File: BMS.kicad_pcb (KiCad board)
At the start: 2 copper layers, 129 parts, among them IC1 AOZ2261NQI-11, IC2 AOZ2261NQI-11, IC2 LM2596DSADJG, IC3 AOZ2261NQI-11, IC4 AOZ2261NQI-11, IC5 AOZ2261NQI-11, IC6 AOZ2261NQI-11, IC7 AOZ2261NQI-11, J1 Conn_01x05_Pin, J10 XT90PB-F, J11 XT90PB-F, J12 XT90PB-F, J2 XT90PB-F, J3 Conn_01x02_Pin, J4 Conn_01x03_Pin, J5 XT90PB-F, J6 XT90PB-F, J7 XT90PB-F, J8 XT90PB-F, J9 XT90PB-F, Q1 BSC028N06LS3, Q2 IRLB3813PBF, U1 BQ76920PW, U2 453-00001R

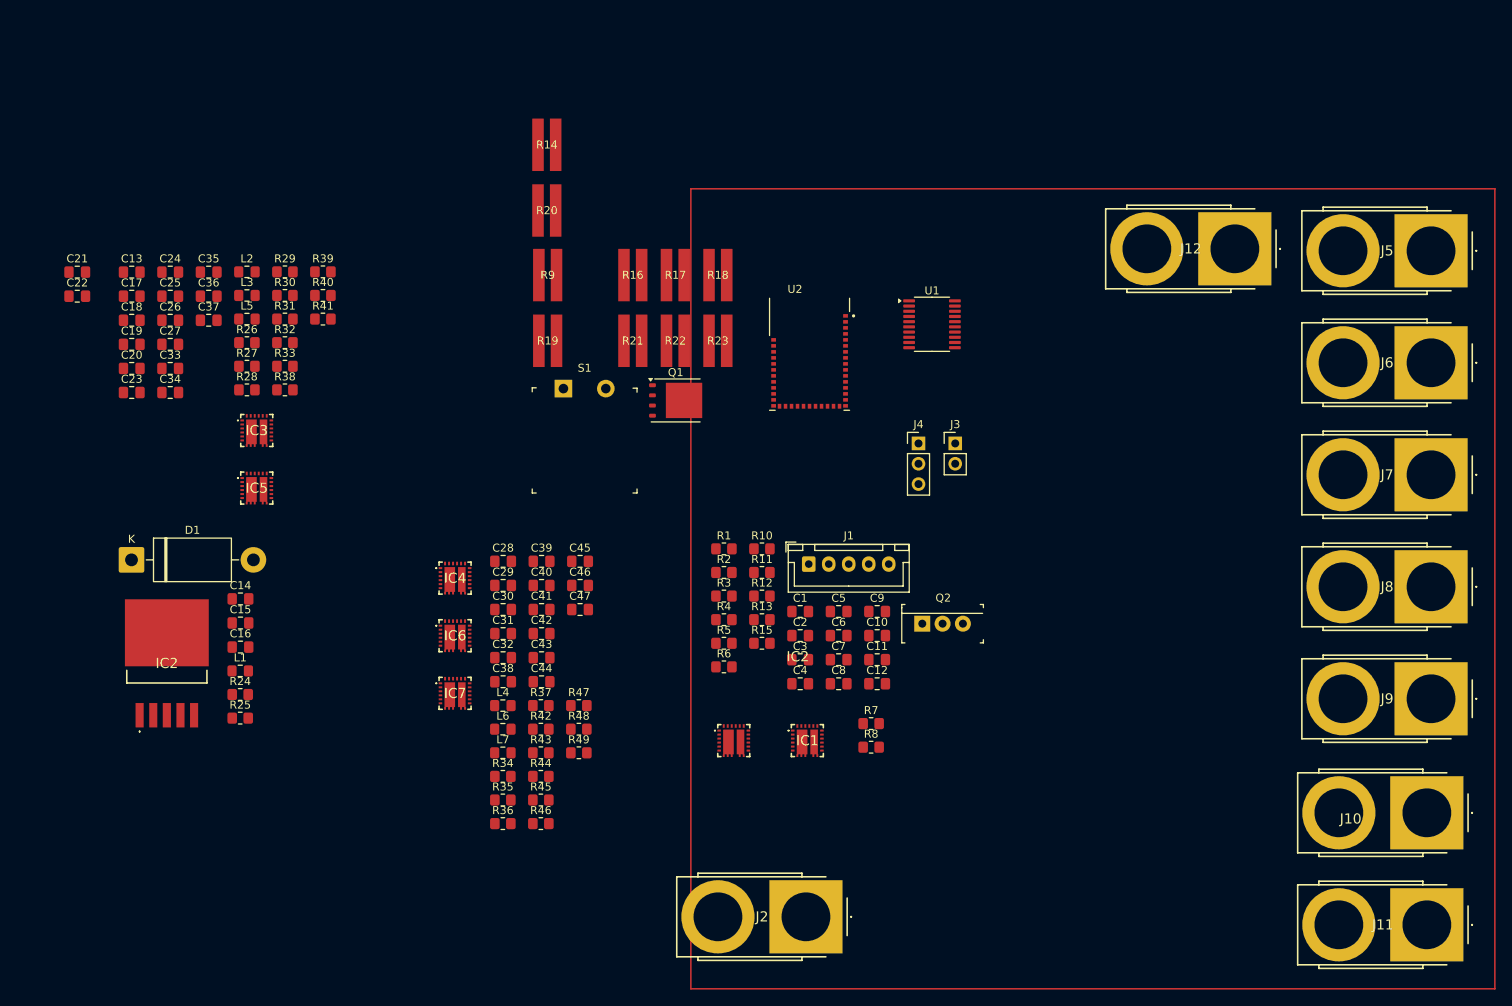
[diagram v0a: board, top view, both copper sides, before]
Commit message: Added output and input caps for buck converters into the schematic. Added components into the project specific library.
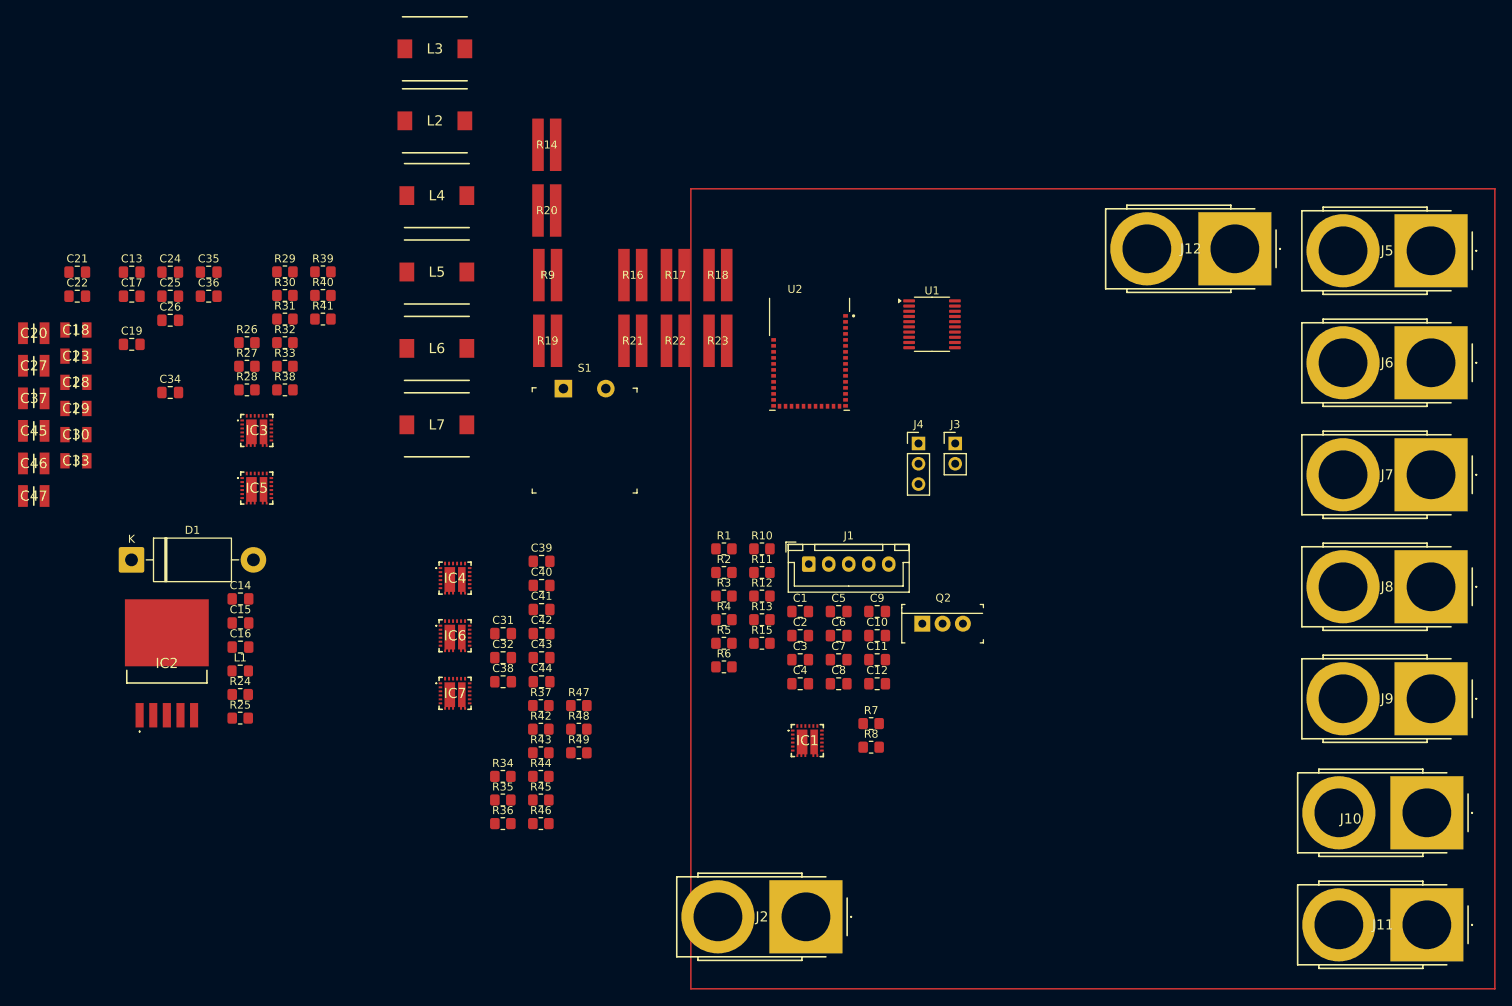
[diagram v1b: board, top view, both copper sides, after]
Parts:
- removed the IC2 at (108.4, 100.5)
- removed Q1: BSC028N06LS3, Package_TO_SOT_SMD:TDSON-8-1
- C18, C23, C28, C29, C30, C33: value 22u -> TMK316BBJ226ML-T; footprint Capacitor_SMD:C_0805_2012Metric_Pad1.18x1.45mm_HandSolder -> TMK316BBJ226ML-T:CAPC3216X190N
- C20, C27, C37, C45, C46, C47: value 22u -> EMK325ABJ107MM-P; footprint Capacitor_SMD:C_0805_2012Metric_Pad1.18x1.45mm_HandSolder -> EMK325ABJ107MM-P:CAPC3225X270N
- L2, L3, L4, L5, L6, L7: value 1u -> HCM1A0805-3R3-R; footprint Inductor_SMD:L_0805_2012Metric_Pad1.15x1.40mm_HandSolder -> HCM1A0805-3R3-R:INDPM8180X540N
- moved C45 70.2 mm to (20.9, 61.8)
- moved C46 70.0 mm to (20.9, 65.8)
- moved C47 69.7 mm to (20.9, 69.9)
- moved L4 64.3 mm to (71.2, 32.4)
- moved C28 57.9 mm to (26.1, 55.7)
- moved C29 57.8 mm to (26.1, 59.0)
- moved C30 57.7 mm to (26.1, 62.2)
- moved L6 48.3 mm to (71.2, 51.5)
- moved L7 41.8 mm to (71.2, 61.0)
- moved L3 38.8 mm to (71.0, 14.0)
- moved L2 30.1 mm to (71.0, 23.0)
- moved L5 24.5 mm to (71.2, 41.9)
- moved C37 23.9 mm to (20.9, 57.7)
- moved C27 17.3 mm to (20.9, 53.6)
- moved C33 16.5 mm to (26.1, 65.5)
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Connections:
- C18 pad 1: PACK+ -> GNDPWR
- C18 pad 2: GNDPWR -> PACK+
- C20 pad 1: 12VOUT -> GNDPWR
- C20 pad 2: GNDPWR -> 12VOUT
- C23 pad 1: PACK+ -> GNDPWR
- C23 pad 2: GNDPWR -> PACK+
- C27 pad 1: 9VOUT -> GNDPWR
- C27 pad 2: GNDPWR -> 9VOUT
- C28 pad 1: PACK+ -> GNDPWR
- C28 pad 2: GNDPWR -> PACK+
- C29 pad 1: PACK+ -> GNDPWR
- C29 pad 2: GNDPWR -> PACK+
- C30 pad 1: PACK+ -> GNDPWR
- C30 pad 2: GNDPWR -> PACK+
- C33 pad 1: PACK+ -> GNDPWR
- C33 pad 2: GNDPWR -> PACK+
- C37 pad 1: 5VOUT -> GNDPWR
- C37 pad 2: GNDPWR -> 5VOUT
- C45 pad 1: 12VOUT -> GNDPWR
- C45 pad 2: GNDPWR -> 12VOUT
- C46 pad 1: 9VOUT -> GNDPWR
- C46 pad 2: GNDPWR -> 9VOUT
- C47 pad 1: 5VOUT -> GNDPWR
- C47 pad 2: GNDPWR -> 5VOUT

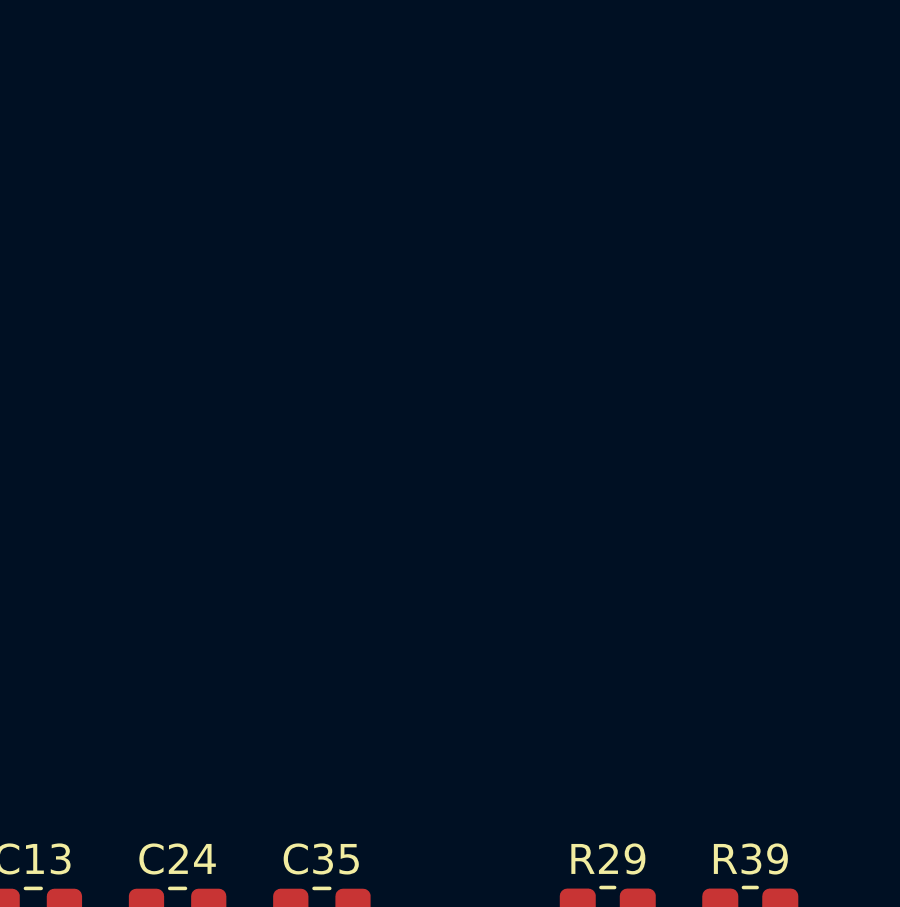
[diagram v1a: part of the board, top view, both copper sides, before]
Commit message: Changed RTon values to get reasonable osscilation frequencies for all the buck converters, added 10K current limit resistors to all the OCS pins, adjusted some net names to be different for the two buck converters at each voltage
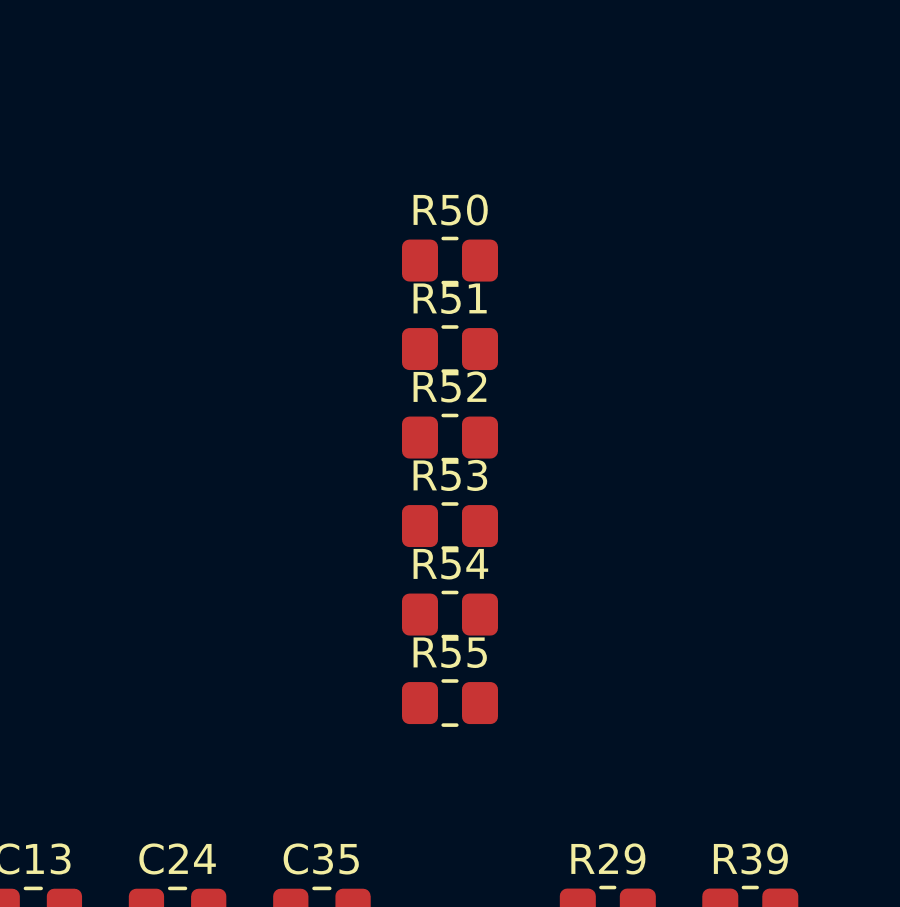
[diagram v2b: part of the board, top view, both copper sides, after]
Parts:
- added R50: 10k, Resistor_SMD:R_0805_2012Metric_Pad1.20x1.40mm_HandSolder, F.Cu at (47.0, 20.2)
- added R51: 10k, Resistor_SMD:R_0805_2012Metric_Pad1.20x1.40mm_HandSolder, F.Cu at (47.0, 23.2)
- added R52: 10k, Resistor_SMD:R_0805_2012Metric_Pad1.20x1.40mm_HandSolder, F.Cu at (47.0, 26.1)
- added R53: 10k, Resistor_SMD:R_0805_2012Metric_Pad1.20x1.40mm_HandSolder, F.Cu at (47.0, 29.1)
- added R54: 10k, Resistor_SMD:R_0805_2012Metric_Pad1.20x1.40mm_HandSolder, F.Cu at (47.0, 32.0)
- added R55: 10k, Resistor_SMD:R_0805_2012Metric_Pad1.20x1.40mm_HandSolder, F.Cu at (47.0, 35.0)
- R27, R34: value 100k -> 1.2M
- R30, R35: value 100k -> 600k
- R36, R38: value 100k -> 333k
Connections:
- IC1 pad 19: unconnected-(IC1-OCS-Pad19) -> /Power Distribution/OCS12_1
- IC3 pad 19: unconnected-(IC3-OCS-Pad19) -> /Power Distribution/OCS9_1
- IC4 pad 19: unconnected-(IC4-OCS-Pad19) -> /Power Distribution/OCS12_2
- IC5 pad 19: unconnected-(IC5-OCS-Pad19) -> /Power Distribution/OCS5_1
- IC6 pad 19: unconnected-(IC6-OCS-Pad19) -> /Power Distribution/OCS9_2
- IC7 pad 19: unconnected-(IC7-OCS-Pad19) -> /Power Distribution/OCS5_2

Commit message: Added A and Bonto the all the net labels and sheet outputs for the pairs of buck converters. Moved the XT90 connector for the battery input to the connectors sectionof the main sheet and renamed the nodes to BAT+ and BAT-. Added some comments clarifying the purpose of some connectors and which grounds go to which device.
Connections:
- net /Power Distribution/OCS12_1 renamed /Power Distribution/OCS12_A
- net /Power Distribution/OCS12_2 renamed /Power Distribution/OCS12_B
- net /Power Distribution/OCS5_1 renamed /Power Distribution/OCS5_A
- net /Power Distribution/OCS5_2 renamed /Power Distribution/OCS5_B
- net /Power Distribution/OCS9_1 renamed /Power Distribution/OCS9_A
- net /Power Distribution/OCS9_2 renamed /Power Distribution/OCS9_B
- net GND1 renamed BAT-
- net PACK+ renamed BAT+
- C19 pad 1: /Power Distribution/LX12 -> /Power Distribution/LX12_A
- C20 pad 2: 12VOUT -> 12VOUT_A
- C24 pad 1: /Power Distribution/LX9 -> /Power Distribution/LX9_A
- C27 pad 2: 9VOUT -> 9VOUT_A
- C31 pad 1: /Power Distribution/LX12 -> /Power Distribution/LX12_B
- C32 pad 1: /Power Distribution/LX9 -> /Power Distribution/LX9_B
- C34 pad 1: /Power Distribution/LX5 -> /Power Distribution/LX5_A
- C37 pad 2: 5VOUT -> 5VOUT_A
- C38 pad 1: /Power Distribution/LX5 -> /Power Distribution/LX5_B
- C45 pad 2: 12VOUT -> 12VOUT_B
- C46 pad 2: 9VOUT -> 9VOUT_B
- C47 pad 2: 5VOUT -> 5VOUT_B
- IC1 pad 1: /PGOOD12 -> /PGOOD12_B
- IC1 pad 10: /Power Distribution/LX12 -> /Power Distribution/LX12_A
- IC1 pad 11: /Power Distribution/LX12 -> /Power Distribution/LX12_A
- IC1 pad 16: /Power Distribution/LX12 -> /Power Distribution/LX12_A
- IC1 pad 17: /Power Distribution/LX12 -> /Power Distribution/LX12_A
- IC1 pad 18: /Power Distribution/LX12 -> /Power Distribution/LX12_A
- IC1 pad 2: /EN12 -> /EN12_B
- IC1 pad 25: /Power Distribution/LX12 -> /Power Distribution/LX12_A
- IC1 pad 5: /Power Distribution/FB12 -> /Power Distribution/FB12_A
- IC3 pad 1: /PGOOD9 -> /PGOOD9_A
- IC3 pad 10: /Power Distribution/LX9 -> /Power Distribution/LX9_A
- IC3 pad 11: /Power Distribution/LX9 -> /Power Distribution/LX9_A
- IC3 pad 16: /Power Distribution/LX9 -> /Power Distribution/LX9_A
- IC3 pad 17: /Power Distribution/LX9 -> /Power Distribution/LX9_A
- IC3 pad 18: /Power Distribution/LX9 -> /Power Distribution/LX9_A
- IC3 pad 2: /EN9 -> /EN9_A
- IC3 pad 25: /Power Distribution/LX9 -> /Power Distribution/LX9_A
- IC3 pad 5: /Power Distribution/FB9 -> /Power Distribution/FB9_A
- IC4 pad 1: /PGOOD12 -> /PGOOD12_A
- IC4 pad 10: /Power Distribution/LX12 -> /Power Distribution/LX12_B
- IC4 pad 11: /Power Distribution/LX12 -> /Power Distribution/LX12_B
- IC4 pad 16: /Power Distribution/LX12 -> /Power Distribution/LX12_B
- IC4 pad 17: /Power Distribution/LX12 -> /Power Distribution/LX12_B
- IC4 pad 18: /Power Distribution/LX12 -> /Power Distribution/LX12_B
- IC4 pad 2: /EN12 -> /EN12_A
- IC4 pad 25: /Power Distribution/LX12 -> /Power Distribution/LX12_B
- IC4 pad 5: /Power Distribution/FB12 -> /Power Distribution/FB12_B
- IC5 pad 1: /PGOOD5 -> /PGOOD5_A
- IC5 pad 10: /Power Distribution/LX5 -> /Power Distribution/LX5_A
- IC5 pad 11: /Power Distribution/LX5 -> /Power Distribution/LX5_A
- IC5 pad 16: /Power Distribution/LX5 -> /Power Distribution/LX5_A
- IC5 pad 17: /Power Distribution/LX5 -> /Power Distribution/LX5_A
- IC5 pad 18: /Power Distribution/LX5 -> /Power Distribution/LX5_A
- IC5 pad 2: /EN5 -> /EN5_A
- IC5 pad 25: /Power Distribution/LX5 -> /Power Distribution/LX5_A
- IC5 pad 5: /Power Distribution/FB5 -> /Power Distribution/FB5_A
- IC6 pad 1: /PGOOD9 -> /PGOOD9_B
- IC6 pad 10: /Power Distribution/LX9 -> /Power Distribution/LX9_B
- IC6 pad 11: /Power Distribution/LX9 -> /Power Distribution/LX9_B
- IC6 pad 16: /Power Distribution/LX9 -> /Power Distribution/LX9_B
- IC6 pad 17: /Power Distribution/LX9 -> /Power Distribution/LX9_B
- IC6 pad 18: /Power Distribution/LX9 -> /Power Distribution/LX9_B
- IC6 pad 2: /EN9 -> /EN9_B
- IC6 pad 25: /Power Distribution/LX9 -> /Power Distribution/LX9_B
- IC6 pad 5: /Power Distribution/FB9 -> /Power Distribution/FB9_B
- IC7 pad 1: /PGOOD5 -> /PGOOD5_B
- IC7 pad 10: /Power Distribution/LX5 -> /Power Distribution/LX5_B
- IC7 pad 11: /Power Distribution/LX5 -> /Power Distribution/LX5_B
- IC7 pad 16: /Power Distribution/LX5 -> /Power Distribution/LX5_B
- IC7 pad 17: /Power Distribution/LX5 -> /Power Distribution/LX5_B
- IC7 pad 18: /Power Distribution/LX5 -> /Power Distribution/LX5_B
- IC7 pad 2: /EN5 -> /EN5_B
- IC7 pad 25: /Power Distribution/LX5 -> /Power Distribution/LX5_B
- IC7 pad 5: /Power Distribution/FB5 -> /Power Distribution/FB5_B
- J10 pad 2: 9VOUT -> 9VOUT_B
- J11 pad 2: 5VOUT -> 5VOUT_B
- J12 pad 2: 5VOUT -> 5VOUT_A
- J7 pad 2: 12VOUT -> 12VOUT_A
- J8 pad 2: 12VOUT -> 12VOUT_B
- J9 pad 2: 9VOUT -> 9VOUT_A
- L2 pad 1: /Power Distribution/LX12 -> /Power Distribution/LX12_A
- L2 pad 2: 12VOUT -> 12VOUT_A
- L3 pad 1: /Power Distribution/LX9 -> /Power Distribution/LX9_A
- L3 pad 2: 9VOUT -> 9VOUT_A
- L4 pad 1: /Power Distribution/LX12 -> /Power Distribution/LX12_B
- L4 pad 2: 12VOUT -> 12VOUT_B
- L5 pad 1: /Power Distribution/LX5 -> /Power Distribution/LX5_A
- L5 pad 2: 5VOUT -> 5VOUT_A
- L6 pad 1: /Power Distribution/LX9 -> /Power Distribution/LX9_B
- L6 pad 2: 9VOUT -> 9VOUT_B
- L7 pad 1: /Power Distribution/LX5 -> /Power Distribution/LX5_B
- L7 pad 2: 5VOUT -> 5VOUT_B
- R26 pad 2: /PGOOD12 -> /PGOOD12_B
- R28 pad 1: /Power Distribution/FB12 -> /Power Distribution/FB12_A
- R28 pad 2: 12VOUT -> 12VOUT_A
- R29 pad 2: /Power Distribution/FB12 -> /Power Distribution/FB12_A
- R31 pad 2: /PGOOD9 -> /PGOOD9_A
- R32 pad 1: /Power Distribution/FB9 -> /Power Distribution/FB9_A
- R32 pad 2: 9VOUT -> 9VOUT_A
- R33 pad 2: /Power Distribution/FB9 -> /Power Distribution/FB9_A
- R37 pad 2: /PGOOD12 -> /PGOOD12_A
- R39 pad 2: /PGOOD5 -> /PGOOD5_A
- R40 pad 1: /Power Distribution/FB5 -> /Power Distribution/FB5_A
- R40 pad 2: 5VOUT -> 5VOUT_A
- R41 pad 2: /Power Distribution/FB5 -> /Power Distribution/FB5_A
- R42 pad 1: +5V -> /Power Distribution/VCC9_2
- R42 pad 2: /PGOOD9 -> /PGOOD9_B
- R43 pad 2: /PGOOD5 -> /PGOOD5_B
- R44 pad 1: /Power Distribution/FB12 -> /Power Distribution/FB12_B
- R44 pad 2: 12VOUT -> 12VOUT_B
- R45 pad 2: /Power Distribution/FB12 -> /Power Distribution/FB12_B
- R46 pad 1: /Power Distribution/FB9 -> /Power Distribution/FB9_B
- R46 pad 2: 9VOUT -> 9VOUT_B
- R47 pad 2: /Power Distribution/FB9 -> /Power Distribution/FB9_B
- R48 pad 1: /Power Distribution/FB5 -> /Power Distribution/FB5_B
- R48 pad 2: 5VOUT -> 5VOUT_B
- R49 pad 2: /Power Distribution/FB5 -> /Power Distribution/FB5_B
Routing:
- net 9VOUT_B: track 0.00 -> 0.74 mm
- net 9VOUT: track 0.74 -> 0.00 mm
